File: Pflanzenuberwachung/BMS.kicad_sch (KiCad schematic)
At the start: 0 parts

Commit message: Update BMS Axel
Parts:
- added C17, C19: C10uF, Capacitor_SMD:C_0805_2012Metric, symbol Device:C
- added C21: C2.2pF, Capacitor_SMD:C_0805_2012Metric, symbol Device:C
- added D2: LED, LED_SMD:LED_0805_2012Metric, symbol Device:LED
- added F1, F2: Fuse, Fuse:Fuse_0805_2012Metric, symbol Device:Fuse
- added J11, J12, J8: ~, Connector_PinHeader_2.54mm:PinHeader_1x02_P2.54mm_Vertical, symbol Connector:Conn_01x02_Pin
- added J6: USB_C_Receptacle_PowerOnly_6P, Connector_USB:USB_C_Receptacle_GCT_USB4135-GF-A_6P_TopMnt_Horizontal, symbol Connector:USB_C_Receptacle_PowerOnly_6P
- added J9: ~, Connector_PinHeader_1.00mm:PinHeader_1x02_P1.00mm_Vertical, symbol Connector:Conn_01x02_Pin
- added R5: R91, Resistor_SMD:R_0805_2012Metric, symbol Device:R
- added R6: R1.87k, Capacitor_SMD:C_0805_2012Metric, symbol Device:R
- added U2: LTC3553, Package_DFN_QFN:QFN-20-1EP_3x3mm_P0.4mm_EP1.65x1.65mm, symbol Battery_Management:LTC3553
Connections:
- new net: D2.2 (A), U2.14 (~{CHRG})
- new net: R6.1, U2.16 (PROG)
- new net: F2.2, U2.17 (BAT)
- new net: C19.1, J11.2 (Pin_2), U2.18 (VOUT)
- new net: C17.1, J8.1 (Pin_1), U2.20 (VBUS)
- new net: J9.1 (Pin_1), U2.4 (~{ON})
- new net: D2.1 (K), R5.1
- new net: F1.1, J8.2 (Pin_2)
- new net: F2.1, J12.2 (Pin_2)
- new net: F1.2, J6.A9 (VBUS), J6.B9 (VBUS)
- new net GND: C17.2, C19.2, C21.2, J12.1 (Pin_1), J6.A12 (GND), J6.B12 (GND), J6.S1 (SHIELD), J9.2 (Pin_2), R5.2, R6.2, U2.15 (NTC), U2.2 (SEQ), U2.21 (GND), U2.5 (LDO_ON), U2.6 (STBY)
- new net Vout 3,8V: C21.1, J11.1 (Pin_1), U2.12 (BVIN), U2.7 (BUCK_ON)

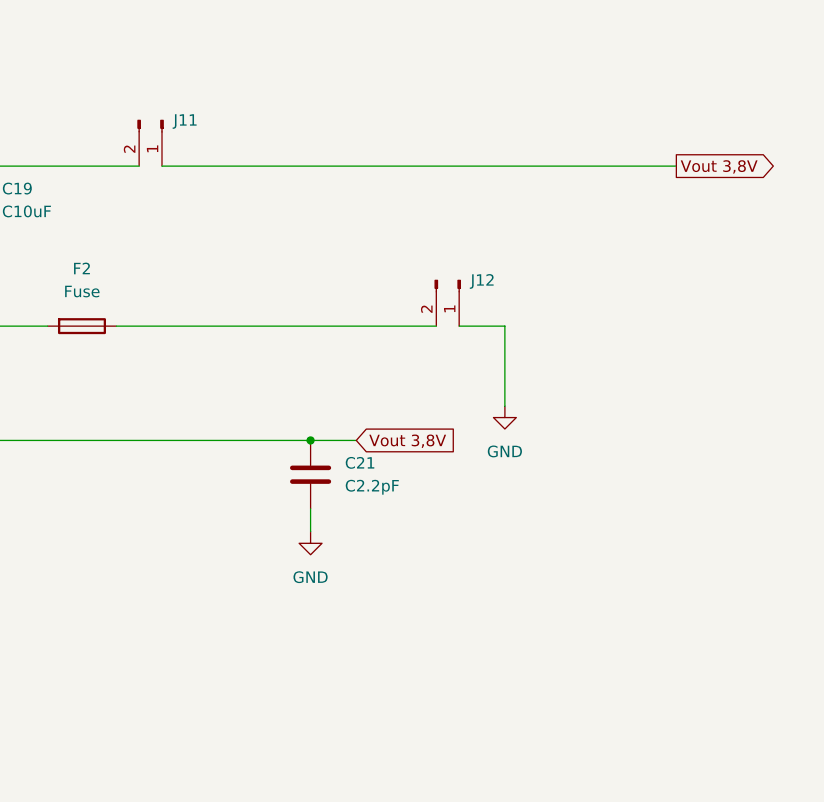
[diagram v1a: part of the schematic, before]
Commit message: Verbindungen hinzugefügt
Microprozessor mit LTE modul  und Sensoren verbungen. Plus Statusleuchte Spannungsversorgung hinzugefügt
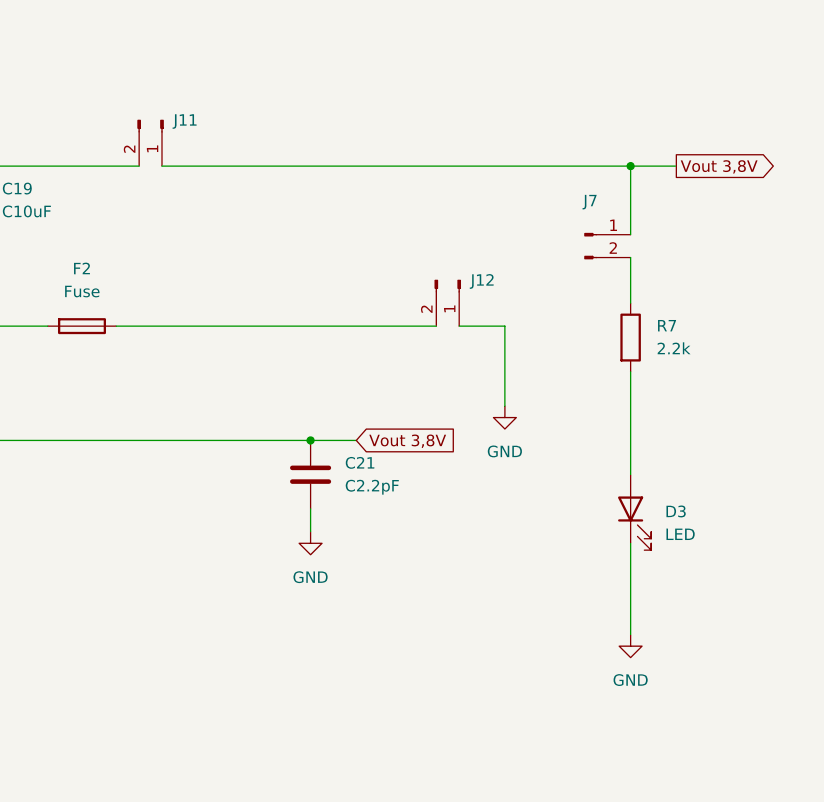
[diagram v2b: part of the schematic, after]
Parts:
- added D3: LED, LED_SMD:LED_0805_2012Metric, symbol Device:LED
- added J7: ~, Connector_PinHeader_2.54mm:PinHeader_1x02_P2.54mm_Vertical, symbol Connector:Conn_01x02_Pin
- added R7: 2.2k, Resistor_SMD:R_0402_1005Metric, symbol Device:R
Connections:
- net GND: now also D3.1 (K)
- net Vout 3,8V: now also J7.1 (Pin_1)
- new net: D3.2 (A), R7.2
- new net: J7.2 (Pin_2), R7.1

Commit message: 1,8V Bereitstellung BMS
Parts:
- added C18, C20: C10pF, Capacitor_SMD:C_0805_2012Metric, symbol Device:C
- added J13: ~, Connector_PinHeader_2.54mm:PinHeader_1x02_P2.54mm_Vertical, symbol Connector:Conn_01x02_Pin
- added L1: L10uH, Inductor_SMD:L_0805_2012Metric, symbol Device:L
- added R10: 2.2k, Resistor_SMD:R_0402_1005Metric, symbol Device:R
- added R9: R464k, Capacitor_SMD:C_0805_2012Metric, symbol Device:R
- J8: footprint Connector_PinHeader_2.54mm:PinHeader_1x02_P2.54mm_Vertical -> Connector_PinHeader_1.00mm:PinHeader_1x02_P1.00mm_Vertical
- J9: footprint Connector_PinHeader_1.00mm:PinHeader_1x02_P1.00mm_Vertical -> Connector_PinHeader_2.54mm:PinHeader_1x02_P2.54mm_Vertical
- R7: value 2.2k -> R590k; footprint Resistor_SMD:R_0402_1005Metric -> Capacitor_SMD:C_0805_2012Metric
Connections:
- net GND: now also J8.2 (Pin_2), C20.2, R9.2; no longer J9.2 (Pin_2)
- net Vout 3,8V: now also J13.1 (Pin_1); no longer J7.1 (Pin_1)
- net at U2.13 (SW): now also L1.2
- net at C17.1, U2.20 (VBUS): now also F1.1, J7.1 (Pin_1), J7.2 (Pin_2); no longer J8.1 (Pin_1)
- net at U2.4 (~{ON}): now also J8.1 (Pin_1); no longer J9.1 (Pin_1)
- net at U2.8 (BUCK_FB): now also R7.2, C18.2, R9.1
- net at D3.2 (A): now also R10.2; no longer R7.2
- net at R7.1: now also J9.2 (Pin_2), C18.1, C20.1, L1.1; no longer J7.2 (Pin_2)
- new net: J13.2 (Pin_2), R10.1
- new net Vbuck 1,8V: J9.1 (Pin_1)

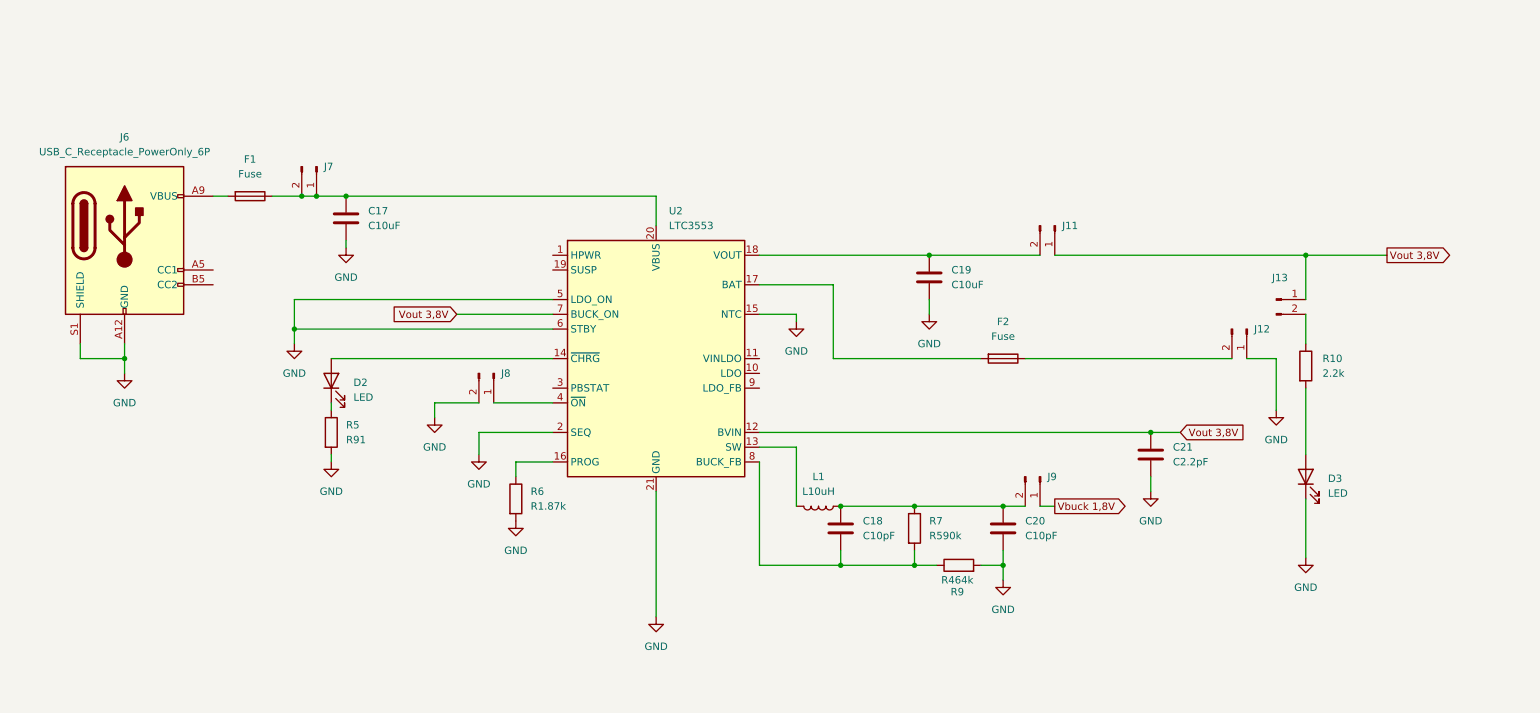
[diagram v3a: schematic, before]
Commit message: PCB Bord
PCB Design und kleiner nicht relevante änderungen
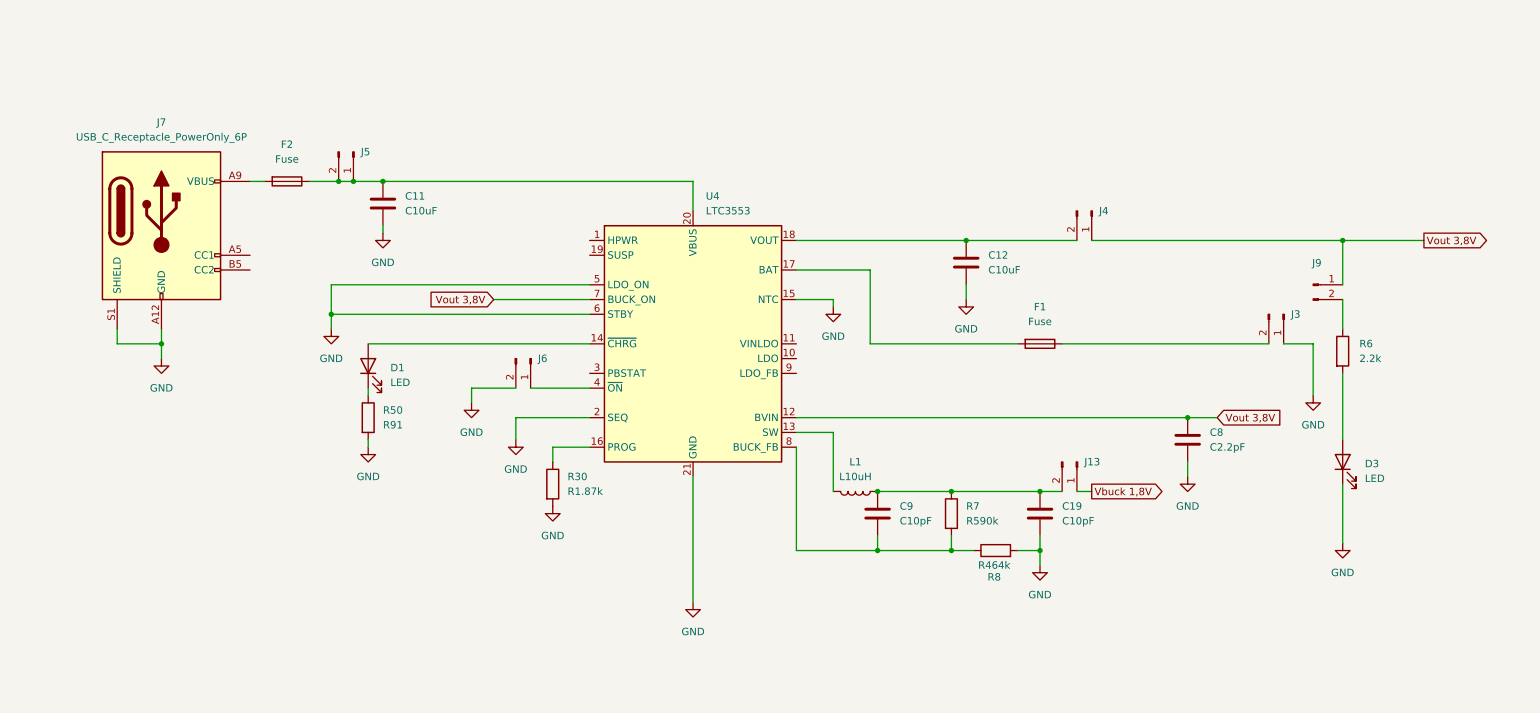
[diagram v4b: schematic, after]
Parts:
- removed C17: C10uF, Capacitor_SMD:C_0805_2012Metric, symbol Device:C
- removed C18, C20: C10pF, Capacitor_SMD:C_0805_2012Metric, symbol Device:C
- removed C21: C2.2pF, Capacitor_SMD:C_0805_2012Metric, symbol Device:C
- removed D2: LED, LED_SMD:LED_0805_2012Metric, symbol Device:LED
- removed J11, J12, J7: ~, Connector_PinHeader_2.54mm:PinHeader_1x02_P2.54mm_Vertical, symbol Connector:Conn_01x02_Pin
- removed J6: USB_C_Receptacle_PowerOnly_6P, Connector_USB:USB_C_Receptacle_GCT_USB4135-GF-A_6P_TopMnt_Horizontal, symbol Connector:USB_C_Receptacle_PowerOnly_6P
- removed J8: ~, Connector_PinHeader_1.00mm:PinHeader_1x02_P1.00mm_Vertical, symbol Connector:Conn_01x02_Pin
- removed R10: 2.2k, Resistor_SMD:R_0402_1005Metric, symbol Device:R
- removed R5: R91, Resistor_SMD:R_0805_2012Metric, symbol Device:R
- removed R9: R464k, Capacitor_SMD:C_0805_2012Metric, symbol Device:R
- removed U2: LTC3553, Package_DFN_QFN:QFN-20-1EP_3x3mm_P0.4mm_EP1.65x1.65mm, symbol Battery_Management:LTC3553
- added C11, C12: C10uF, Capacitor_SMD:C_0805_2012Metric, symbol Device:C
- added C8: C2.2pF, Capacitor_SMD:C_0805_2012Metric, symbol Device:C
- added C9: C10pF, Capacitor_SMD:C_0805_2012Metric, symbol Device:C
- added D1: LED, LED_SMD:LED_0805_2012Metric, symbol Device:LED
- added J3, J4, J5: ~, Connector_PinHeader_2.54mm:PinHeader_1x02_P2.54mm_Vertical, symbol Connector:Conn_01x02_Pin
- added J6: ~, Connector_PinHeader_1.00mm:PinHeader_1x02_P1.00mm_Vertical, symbol Connector:Conn_01x02_Pin
- added J7: USB_C_Receptacle_PowerOnly_6P, Connector_USB:USB_C_Receptacle_GCT_USB4135-GF-A_6P_TopMnt_Horizontal, symbol Connector:USB_C_Receptacle_PowerOnly_6P
- added R30: R1.87k, Capacitor_SMD:C_0805_2012Metric, symbol Device:R
- added R50: R91, Resistor_SMD:R_0805_2012Metric, symbol Device:R
- added R8: R464k, Capacitor_SMD:C_0805_2012Metric, symbol Device:R
- added U4: LTC3553, Package_DFN_QFN:QFN-20-1EP_3x3mm_P0.4mm_EP1.65x1.65mm, symbol Battery_Management:LTC3553
- C19: value C10uF -> C10pF
- R6: value R1.87k -> 2.2k; footprint Capacitor_SMD:C_0805_2012Metric -> Resistor_SMD:R_0402_1005Metric
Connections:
- net GND: now also C11.2, C12.2, C8.2, J3.1 (Pin_1), J6.2 (Pin_2), J7.A12 (GND), J7.B12 (GND), J7.S1 (SHIELD), R30.2, R50.2, R8.2, U4.15 (NTC), U4.2 (SEQ), U4.21 (GND), U4.5 (LDO_ON), U4.6 (STBY); no longer R6.2
- net Vbuck 1,8V: now also J13.1 (Pin_1); no longer J9.1 (Pin_1)
- net Vout 3,8V: now also J9.1 (Pin_1), C8.1, J4.1 (Pin_1), U4.12 (BVIN), U4.7 (BUCK_ON); no longer J13.1 (Pin_1)
- net at L1.1, R7.1: now also C19.1, J13.2 (Pin_2), C9.1; no longer J9.2 (Pin_2)
- net at R7.2: now also C9.2, R8.1, U4.8 (BUCK_FB)
- net at F2.1: now also C11.1, J5.1 (Pin_1), J5.2 (Pin_2), U4.20 (VBUS)
- net at F2.2: now also J7.A9 (VBUS), J7.B9 (VBUS)
- net at F1.1: now also J3.2 (Pin_2)
- net at F1.2: now also U4.17 (BAT)
- net at D3.2 (A): now also R6.2
- net at R6.1: now also J9.2 (Pin_2)
- net at L1.2: now also U4.13 (SW)
- new net: D1.2 (A), U4.14 (~{CHRG})
- new net: R30.1, U4.16 (PROG)
- new net: C12.1, J4.2 (Pin_2), U4.18 (VOUT)
- new net: J6.1 (Pin_1), U4.4 (~{ON})
- new net: D1.1 (K), R50.1

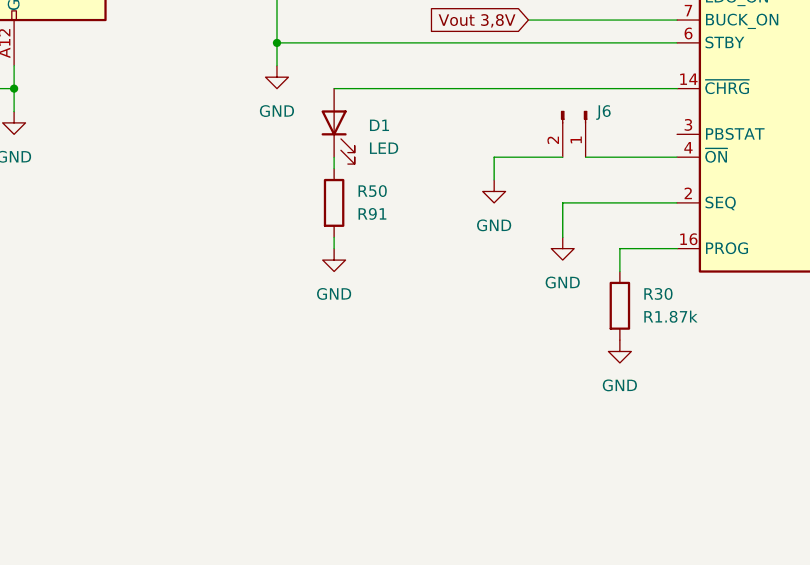
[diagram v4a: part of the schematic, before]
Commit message: Änderungen eintragen
Änderungen an Platine nachtragen: Booth Pin mit GND Verbunden und 3,3V mit Vorwiderstand auf Statuslampe Laden des BMS gelegt
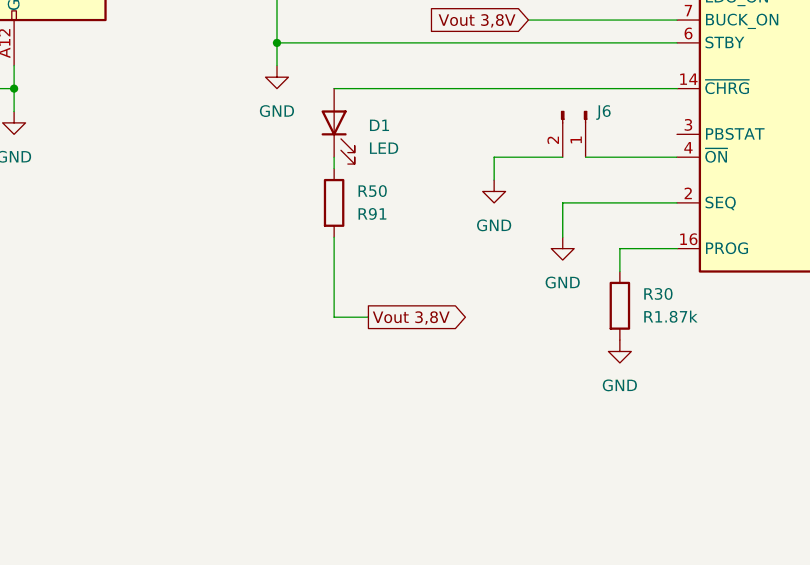
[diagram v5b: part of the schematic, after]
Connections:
- net GND: no longer R50.2
- net Vout 3,8V: now also R50.2
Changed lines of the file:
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@@
+	(wire
+		(pts
+			(xy 82.55 92.71) (xy 82.55 101.6)
+		)
+		(stroke
+			(width 0)
+			(type default)
+		)
+	)
 	(wire
 		(pts
@@
 	(wire
 		(pts
+			(xy 86.36 101.6) (xy 82.55 101.6)
+		)
+		(stroke
+			(width 0)
+			(type default)
+		)
+	)
+	(wire
+		(pts
 			(xy 250.19 58.42) (xy 264.16 58.42)
 		)
@@
 		(pts
 			(xy 201.93 76.2) (xy 237.49 76.2)
-		)
-		(stroke
-			(width 0)
-			(type default)
-		)
-	)
-	(wire
-		(pts
-			(xy 82.55 92.71) (xy 82.55 93.98)
 		)
 		(stroke
@@
 	)
 	(global_label "Vout 3,8V"
+		(shape output)
+		(at 86.36 101.6 0)
+		(fields_autoplaced yes)
+		(effects
+			(font
+				(size 1.27 1.27)
+			)
+			(justify left)
+		)
+		(property "Intersheetrefs" "${INTERSHEET_REFS}"
+			(at 98.5375 101.6 0)
+			(effects
+				(font
+					(size 1.27 1.27)
+				)
+				(justify left)
+				(hide yes)
+			)
+		)
+	)
+	(global_label "Vout 3,8V"
 		(shape input)
 		(at 228.6 88.9 0)
@@
 					(unit 1)
 				)
-			)
-		)
-	)
-	(symbol
-		(lib_id "power:GND")
-		(at 82.55 93.98 0)
-		(unit 1)
-		(exclude_from_sim no)
-		(in_bom yes)
-		(on_board yes)
-		(dnp no)
-		(fields_autoplaced yes)
-		(property "Reference" "#PWR028"
-			(at 82.55 100.33 0)
-			(effects
-				(font
-					(size 1.27 1.27)
-				)
-				(hide yes)
-			)
-		)
-		(property "Value" "GND"
-			(at 82.55 99.06 0)
-			(effects
-				(font
-					(size 1.27 1.27)
-				)
-			)
-		)
-		(property "Footprint" ""
-			(at 82.55 93.98 0)
-			(effects
-				(font
-					(size 1.27 1.27)
-				)
-				(hide yes)
-			)
-		)
-		(property "Datasheet" ""
-			(at 82.55 93.98 0)
-			(effects
-				(font
-					(size 1.27 1.27)
-				)
-				(hide yes)
-			)
-		)
-		(property "Description" "Power symbol creates a global label with name \"GND\" , ground"
-			(at 82.55 93.98 0)
-			(effects
-				(font
-					(size 1.27 1.27)
-				)
-				(hide yes)
-			)
-		)
-		(pin "1"
-		)
-		(instances
-			(project "Pflanzenueberwachung"
-				(path "/ef77ed57-ccc0-485d-b54a-c11bf4a81eae/09bcb73f-3591-4543-800f-2d48de79aa09"
-					(reference "#PWR028")
-					(unit 1)
-				)
